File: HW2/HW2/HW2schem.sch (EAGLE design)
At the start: 21 parts, among them J1 USB_MINI-B_SMT

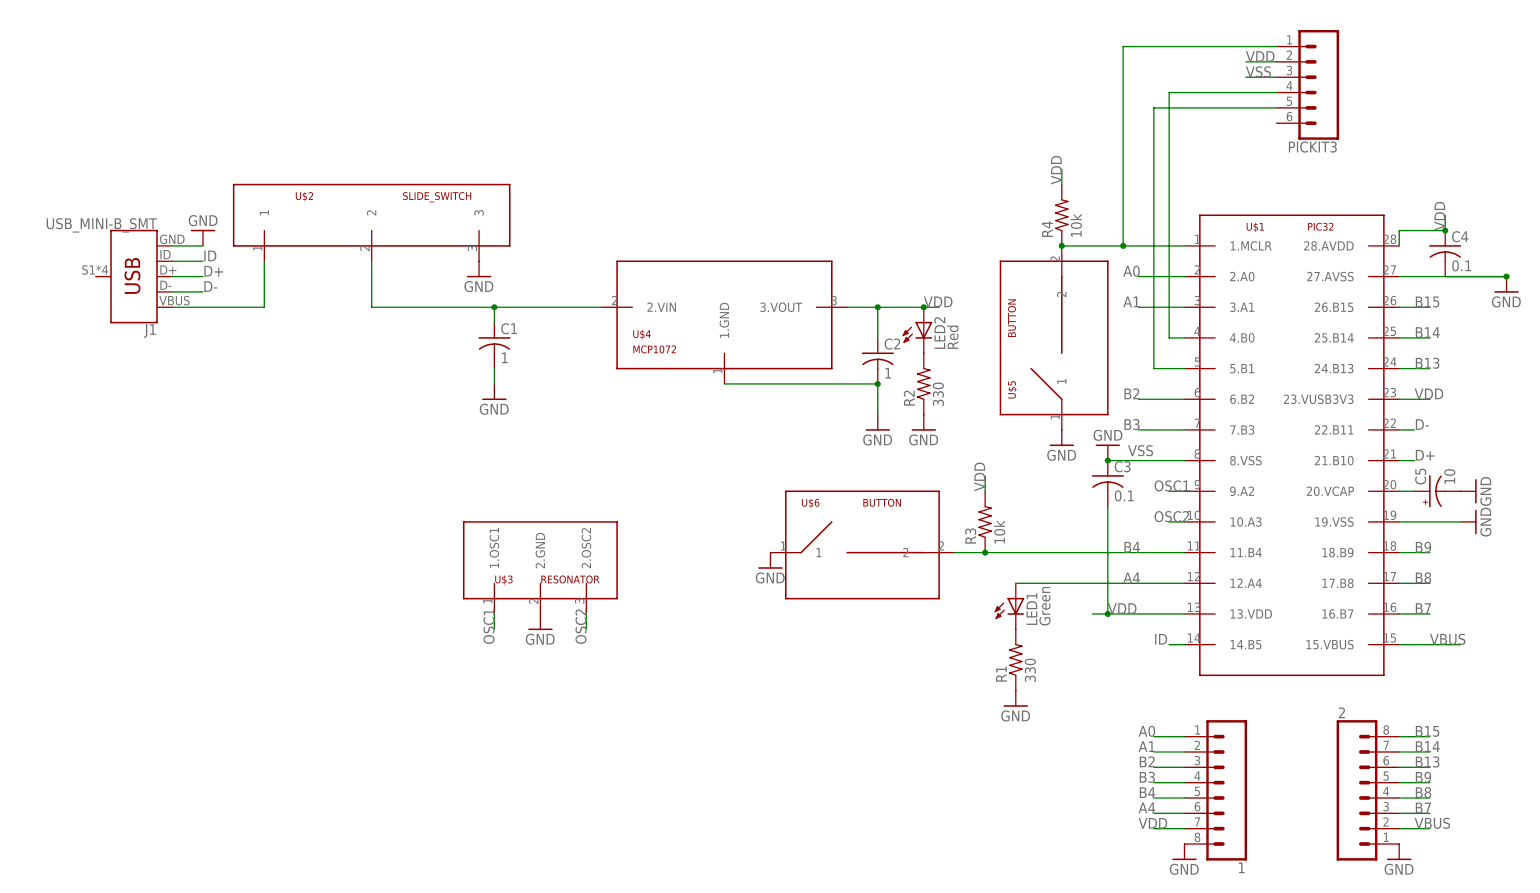
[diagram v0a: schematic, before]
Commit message: Updated Library and schematic based on released video
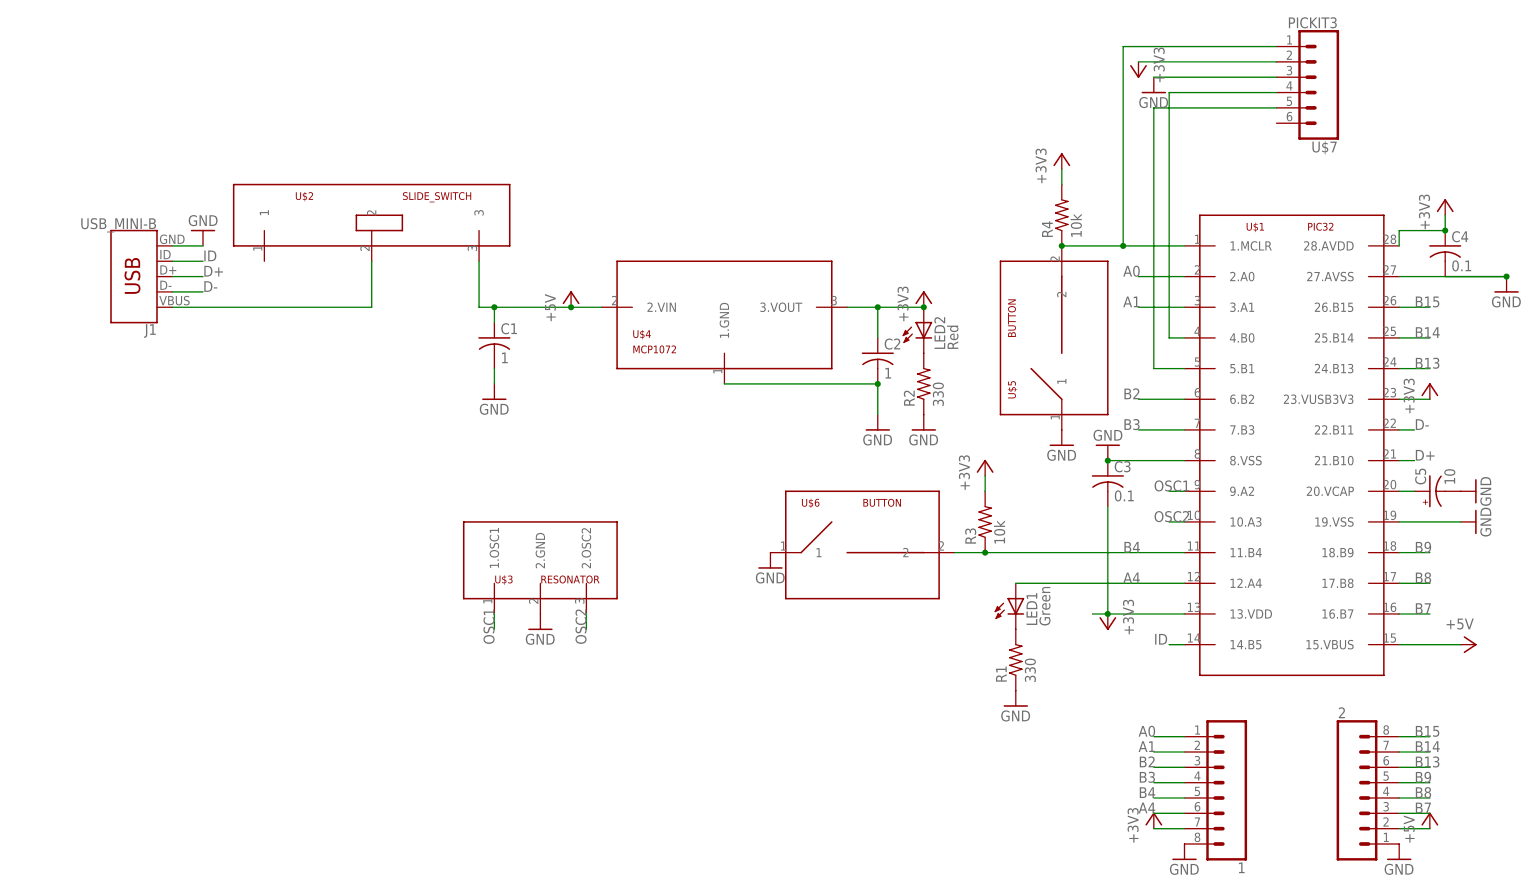
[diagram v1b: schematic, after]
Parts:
- removed PICKIT3: (no value), HW2Lib:CONN_06LONGPADS
- added U$7: PICKIT3, HW2Lib:PICKIT3
- J1: value USB_MINI-B_SMT -> USB_MINI-B; device HW2Lib:USB_MINI-B_SMT -> HW2Lib:USB_MINI-B
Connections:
- removed net VBUS: 2.2, C1.1, U$1.15.VBUS, U$2.2, U$4.2.VIN
- removed net VDD: 1.7, C2.1, C3.2, C4.1, LED2.A, PICKIT3.2, R3.2, R4.2, U$1.13.VDD, U$1.23.VUSB3V3, U$1.28.AVDD, U$4.3.VOUT
- new net +3V3: 1.7, C2.1, C3.2, C4.1, LED2.A, R3.2, R4.2, U$1.13.VDD, U$1.23.VUSB3V3, U$1.28.AVDD, U$4.3.VOUT, U$7.2
- new net +5V: 2.2, C1.1, U$1.15.VBUS, U$2.3, U$4.2.VIN
- net GND: now also U$7.3; no longer U$2.3
- net N$10: now also U$7.4; no longer PICKIT3.4
- net N$11: now also U$7.5; no longer PICKIT3.5
- net N$2: now also U$7.1; no longer PICKIT3.1
- net N$7: now also U$2.2; no longer U$2.1
- net VSS: no longer PICKIT3.3

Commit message: Rearranged board
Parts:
- R1, R2, R3, R4: device HW2Lib:R-US_0309/12 -> HW2Lib:R-US_0204/7
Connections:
- removed net VSS: C3.1, U$1.8.VSS
- net GND: now also C3.1, U$1.8.VSS
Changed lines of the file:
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@@
 <part name="LED1" library="HW2Lib" deviceset="LED" device="3MM" value="Green"/>
 <part name="LED2" library="HW2Lib" deviceset="LED" device="3MM" value="Red"/>
-<part name="R1" library="HW2Lib" deviceset="R-US_" device="0309/12" value="330"/>
-<part name="R2" library="HW2Lib" deviceset="R-US_" device="0309/12" value="330"/>
-<part name="R3" library="HW2Lib" deviceset="R-US_" device="0309/12" value="10k"/>
 <part name="C1" library="HW2Lib" deviceset="C-US" device="025-024X044" value="1"/>
 <part name="C2" library="HW2Lib" deviceset="C-US" device="025-024X044" value="1"/>
@@
 <part name="C4" library="HW2Lib" deviceset="C-US" device="025-024X044" value="0.1"/>
 <part name="C5" library="HW2Lib" deviceset="CPOL-US" device="B45181A" value="10"/>
-<part name="R4" library="HW2Lib" deviceset="R-US_" device="0309/12" value="10k"/>
 <part name="GND1" library="HW2Lib" deviceset="GND" device=""/>
 <part name="GND2" library="HW2Lib" deviceset="GND" device=""/>
@@
 <part name="P+3" library="supply1" deviceset="+5V" device=""/>
 <part name="U$7" library="HW2Lib" deviceset="PICKIT3" device=""/>
+<part name="R2" library="HW2Lib" deviceset="R-US_" device="0204/7" value="330"/>
+<part name="R4" library="HW2Lib" deviceset="R-US_" device="0204/7" value="10k"/>
+<part name="R3" library="HW2Lib" deviceset="R-US_" device="0204/7" value="10k"/>
+<part name="R1" library="HW2Lib" deviceset="R-US_" device="0204/7" value="330"/>
 </parts>
 <sheets>
@@
 <instance part="LED1" gate="G$1" x="-22.86" y="-17.78"/>
 <instance part="LED2" gate="G$1" x="-38.1" y="27.94"/>
-<instance part="R1" gate="G$1" x="-22.86" y="-27.94" rot="R90"/>
-<instance part="R2" gate="G$1" x="-38.1" y="17.78" rot="R90"/>
-<instance part="R3" gate="G$1" x="-27.94" y="-5.08" rot="R90"/>
 <instance part="C1" gate="G$1" x="-109.22" y="25.4"/>
 <instance part="C2" gate="G$1" x="-45.72" y="22.86"/>
@@
 <instance part="C4" gate="G$1" x="48.26" y="40.64"/>
 <instance part="C5" gate="G$1" x="45.72" y="0" rot="R90"/>
-<instance part="R4" gate="G$1" x="-15.24" y="45.72" rot="R90"/>
 <instance part="GND1" gate="1" x="-157.48" y="43.18" rot="R180"/>
 <instance part="GND2" gate="1" x="-38.1" y="10.16"/>
@@
 <instance part="P+1" gate="1" x="-96.52" y="33.02"/>
 <instance part="+3V1" gate="G$1" x="-38.1" y="33.02"/>
-<instance part="+3V2" gate="G$1" x="0" y="-53.34"/>
-<instance part="P+2" gate="1" x="45.72" y="-53.34"/>
+<instance part="+3V2" gate="G$1" x="-5.08" y="-53.34"/>
+<instance part="P+2" gate="1" x="48.26" y="-53.34"/>
 <instance part="+3V3" gate="G$1" x="-15.24" y="55.88"/>
 <instance part="+3V4" gate="G$1" x="-27.94" y="5.08"/>
@@
 <instance part="+3V8" gate="G$1" x="45.72" y="17.78"/>
 <instance part="P+3" gate="1" x="53.34" y="-25.4" rot="R270"/>
-<instance part="U$7" gate="G$1" x="25.4" y="68.58" rot="R180"/>
+<instance part="U$7" gate="G$1" x="25.4" y="71.12" rot="R180"/>
+<instance part="R2" gate="G$1" x="-38.1" y="17.78" rot="R90"/>
+<instance part="R4" gate="G$1" x="-15.24" y="45.72" rot="R90"/>
+<instance part="R3" gate="G$1" x="-27.94" y="-5.08" rot="R90"/>
+<instance part="R1" gate="G$1" x="-22.86" y="-27.94" rot="R90"/>
 </instances>
 <busses>
@@
 </segment>
 <segment>
-<pinref part="R2" gate="G$1" pin="1"/>
-<pinref part="GND2" gate="1" pin="GND"/>
-</segment>
-<segment>
-<pinref part="R1" gate="G$1" pin="1"/>
-<pinref part="GND10" gate="1" pin="GND"/>
-</segment>
-<segment>
 <pinref part="U$6" gate="G$1" pin="1"/>
 <pinref part="GND9" gate="1" pin="GND"/>
@@
 <pinref part="U$7" gate="G$1" pin="3"/>
 </segment>
+<segment>
+<pinref part="GND2" gate="1" pin="GND"/>
+<pinref part="R2" gate="G$1" pin="1"/>
+</segment>
+<segment>
+<pinref part="GND10" gate="1" pin="GND"/>
+<pinref part="R1" gate="G$1" pin="1"/>
+</segment>
+<segment>
+<pinref part="GND7" gate="1" pin="GND"/>
+<pinref part="C3" gate="G$1" pin="1"/>
+<pinref part="U$1" gate="G$1" pin="8.VSS"/>
+<wire x1="5.08" y1="5.08" x2="-7.62" y2="5.08" width="0.1524" layer="91"/>
+<junction x="-7.62" y="5.08"/>
+</segment>
 </net>
 <net name="N$2" class="0">
 <segment>
-<pinref part="R4" gate="G$1" pin="1"/>
 <pinref part="U$5" gate="G$1" pin="2"/>
 <pinref part="U$1" gate="G$1" pin="1.MCLR"/>
 <wire x1="5.08" y1="40.64" x2="-5.08" y2="40.64" width="0.1524" layer="91"/>
-<junction x="-15.24" y="40.64"/>
 <wire x1="-5.08" y1="40.64" x2="-15.24" y2="40.64" width="0.1524" layer="91"/>
 <wire x1="20.32" y1="73.66" x2="-5.08" y2="73.66" width="0.1524" layer="91"/>
@@
 <junction x="-5.08" y="40.64"/>
 <pinref part="U$7" gate="G$1" pin="1"/>
+<pinref part="R4" gate="G$1" pin="1"/>
+<junction x="-15.24" y="40.64"/>
 </segment>
 </net>
@@
 <pinref part="C5" gate="G$1" pin="+"/>
 <wire x1="43.18" y1="0" x2="40.64" y2="0" width="0.1524" layer="91"/>
-</segment>
-</net>
-<net name="N$1" class="0">
-<segment>
-<pinref part="LED2" gate="G$1" pin="C"/>
-<pinref part="R2" gate="G$1" pin="2"/>
-</segment>
-</net>
-<net name="N$4" class="0">
-<segment>
-<pinref part="LED1" gate="G$1" pin="C"/>
-<pinref part="R1" gate="G$1" pin="2"/>
 </segment>
 </net>
@@
 <segment>
 <pinref part="U$6" gate="G$1" pin="2"/>
+<pinref part="U$1" gate="G$1" pin="11.B4"/>
+<wire x1="-33.02" y1="-10.16" x2="-27.94" y2="-10.16" width="0.1524" layer="91"/>
+<label x="-5.08" y="-10.16" size="1.778" layer="95"/>
 <pinref part="R3" gate="G$1" pin="1"/>
-<wire x1="-27.94" y1="-10.16" x2="-33.02" y2="-10.16" width="0.1524" layer="91"/>
-<pinref part="U$1" gate="G$1" pin="11.B4"/>
 <wire x1="-27.94" y1="-10.16" x2="5.08" y2="-10.16" width="0.1524" layer="91"/>
 <junction x="-27.94" y="-10.16"/>
-<label x="-5.08" y="-10.16" size="1.778" layer="95"/>
 </segment>
 <segment>
@@
 <wire x1="-129.54" y1="38.1" x2="-129.54" y2="30.48" width="0.1524" layer="91"/>
 <wire x1="-129.54" y1="30.48" x2="-162.56" y2="30.48" width="0.1524" layer="91"/>
-</segment>
-</net>
-<net name="VSS" class="0">
-<segment>
-<pinref part="GND7" gate="1" pin="GND"/>
-<pinref part="C3" gate="G$1" pin="1"/>
-<pinref part="U$1" gate="G$1" pin="8.VSS"/>
-<wire x1="5.08" y1="5.08" x2="-7.62" y2="5.08" width="0.1524" layer="91"/>
-<junction x="-7.62" y="5.08"/>
 </segment>
 </net>
@@
 <segment>
 <pinref part="2" gate="G$1" pin="2"/>
-<wire x1="40.64" y1="-55.88" x2="45.72" y2="-55.88" width="0.1524" layer="91"/>
+<wire x1="40.64" y1="-55.88" x2="48.26" y2="-55.88" width="0.1524" layer="91"/>
 <pinref part="P+2" gate="1" pin="+5V"/>
 </segment>
@@
 <segment>
 <pinref part="1" gate="G$1" pin="7"/>
-<wire x1="5.08" y1="-55.88" x2="0" y2="-55.88" width="0.1524" layer="91"/>
+<wire x1="5.08" y1="-55.88" x2="-5.08" y2="-55.88" width="0.1524" layer="91"/>
 <pinref part="+3V2" gate="G$1" pin="+3V3"/>
 </segment>
 <segment>
-<pinref part="R4" gate="G$1" pin="2"/>
 <wire x1="-15.24" y1="50.8" x2="-15.24" y2="53.34" width="0.1524" layer="91"/>
 <pinref part="+3V3" gate="G$1" pin="+3V3"/>
-</segment>
-<segment>
-<pinref part="R3" gate="G$1" pin="2"/>
+<pinref part="R4" gate="G$1" pin="2"/>
+</segment>
+<segment>
 <wire x1="-27.94" y1="0" x2="-27.94" y2="2.54" width="0.1524" layer="91"/>
 <pinref part="+3V4" gate="G$1" pin="+3V3"/>
+<pinref part="R3" gate="G$1" pin="2"/>
 </segment>
 <segment>
@@
 </segment>
 </net>
+<net name="N$1" class="0">
+<segment>
+<pinref part="LED2" gate="G$1" pin="C"/>
+<pinref part="R2" gate="G$1" pin="2"/>
+</segment>
+</net>
+<net name="N$4" class="0">
+<segment>
+<pinref part="LED1" gate="G$1" pin="C"/>
+<pinref part="R1" gate="G$1" pin="2"/>
+</segment>
+</net>

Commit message: Finished tentative board, added sick logo
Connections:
- net +3V3: now also U$7.4.B0; no longer U$7.2
- net GND: now also U$7.3.GND; no longer U$7.3
- net N$10: now also U$7.2.VDD; no longer U$7.4
- net N$11: now also U$7.1.MCLR; no longer U$7.5
- net N$2: now also U$7.5.B1; no longer U$7.1
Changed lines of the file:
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@@
 <wire x1="20.32" y1="68.58" x2="0" y2="68.58" width="0.1524" layer="91"/>
 <pinref part="GND13" gate="1" pin="GND"/>
-<pinref part="U$7" gate="G$1" pin="3"/>
+<pinref part="U$7" gate="G$1" pin="3.GND"/>
 </segment>
 <segment>
@@
 <wire x1="-5.08" y1="73.66" x2="-5.08" y2="40.64" width="0.1524" layer="91"/>
 <junction x="-5.08" y="40.64"/>
-<pinref part="U$7" gate="G$1" pin="1"/>
+<pinref part="U$7" gate="G$1" pin="5.B1"/>
 <pinref part="R4" gate="G$1" pin="1"/>
 <junction x="-15.24" y="40.64"/>
@@
 <wire x1="2.54" y1="25.4" x2="2.54" y2="66.04" width="0.1524" layer="91"/>
 <wire x1="2.54" y1="66.04" x2="20.32" y2="66.04" width="0.1524" layer="91"/>
-<pinref part="U$7" gate="G$1" pin="4"/>
+<pinref part="U$7" gate="G$1" pin="2.VDD"/>
 </segment>
 </net>
@@
 <wire x1="0" y1="20.32" x2="0" y2="63.5" width="0.1524" layer="91"/>
 <wire x1="0" y1="63.5" x2="20.32" y2="63.5" width="0.1524" layer="91"/>
-<pinref part="U$7" gate="G$1" pin="5"/>
+<pinref part="U$7" gate="G$1" pin="1.MCLR"/>
 </segment>
 </net>
@@
 <wire x1="20.32" y1="71.12" x2="-2.54" y2="71.12" width="0.1524" layer="91"/>
 <pinref part="+3V5" gate="G$1" pin="+3V3"/>
-<pinref part="U$7" gate="G$1" pin="2"/>
-</segment>
-<segment>
+<pinref part="U$7" gate="G$1" pin="4.B0"/>
+</segment>
+<segment>
